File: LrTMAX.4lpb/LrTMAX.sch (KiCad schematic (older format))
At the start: 124 parts, among them J1 USB_C_Receptacle_USB2.0, J2 SM06B-SRSS-TB, Q1 2N7002, SW1 Tact_SW_8mm, SW10 EC11_SMD, SW11 EC11_SMD, SW12 EC11_SMD, SW13 EC11_SMD, SW14 EC11_SMD, SW15 EC11_SMD, SW16 EC11_SMD, SW17 EC11_SMD, SW2 Tact_SW_8mm, SW3 Tact_SW_8mm, SW4 Tact_SW_8mm, SW5 Tact_SW_8mm, SW6 Tact_SW_8mm, SW7 Tact_SW_8mm, SW8 Tact_SW_8mm, U1 STM32F072C8Tx, U3 SSD1306_OLED_0.91, U4 SPX3819M5-L3-3TR

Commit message: 0.55-pre3
Fix de-chatter cap. values to 22nF -> 100nF
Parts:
- C10, C11, C12, C13, C14, C15, C16, C17, C18, C19, C20, C21, C22, C23, C24, C25: value 22n -> 100n
- C30, C43, C44, C45: value 0.1u -> 100n
- C40, C41, C55: value 10n -> 100n
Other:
- moved on the sheet: C30
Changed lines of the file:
@@
 U 1 1 5C490EFE
 P 8000 1950
-F 0 "C40" H 8115 1996 50  0000 L CNN
-F 1 "10n" H 8115 1905 50  0000 L CNN
+F 0 "C40" H 7700 2000 50  0000 L CNN
+F 1 "100n" H 7700 1900 50  0000 L CNN
 F 2 "Capacitor_SMD:C_0603_1608Metric" H 8038 1800 50  0001 C CNN
 F 3 "~" H 8000 1950 50  0001 C CNN
@@
 P 9000 1600
 F 0 "C43" V 8950 1400 50  0000 C CNN
-F 1 "0.1u" V 8950 1750 50  0000 C CNN
+F 1 "100n" V 8950 1750 50  0000 C CNN
 F 2 "Capacitor_SMD:C_0603_1608Metric" H 9038 1450 50  0001 C CNN
 F 3 "~" H 9000 1600 50  0001 C CNN
@@
 P 9000 1900
 F 0 "C44" V 8950 1700 50  0000 C CNN
-F 1 "0.1u" V 8950 2050 50  0000 C CNN
+F 1 "100n" V 8950 2050 50  0000 C CNN
 F 2 "Capacitor_SMD:C_0603_1608Metric" H 9038 1750 50  0001 C CNN
 F 3 "~" H 9000 1900 50  0001 C CNN
@@
 P 9000 2200
 F 0 "C45" V 8950 2000 50  0000 C CNN
-F 1 "0.1u" V 8950 2350 50  0000 C CNN
+F 1 "100n" V 8950 2350 50  0000 C CNN
 F 2 "Capacitor_SMD:C_0603_1608Metric" H 9038 2050 50  0001 C CNN
 F 3 "~" H 9000 2200 50  0001 C CNN
@@
 P 9000 1200
 F 0 "C41" V 8950 1000 50  0000 C CNN
-F 1 "10n" V 8950 1350 50  0000 C CNN
+F 1 "100n" V 8950 1350 50  0000 C CNN
 F 2 "Capacitor_SMD:C_0603_1608Metric" H 9038 1050 50  0001 C CNN
 F 3 "~" H 9000 1200 50  0001 C CNN
@@
 L LrE-6-rescue:GND-power #PWR0104
 U 1 1 5C494D8B
-P 9250 2600
-F 0 "#PWR0104" H 9250 2350 50  0001 C CNN
-F 1 "GND" H 9255 2427 50  0000 C CNN
-F 2 "" H 9250 2600 50  0001 C CNN
-F 3 "" H 9250 2600 50  0001 C CNN
-	1    9250 2600
+P 9300 2500
+F 0 "#PWR0104" H 9300 2250 50  0001 C CNN
+F 1 "GND" H 9305 2327 50  0000 C CNN
+F 2 "" H 9300 2500 50  0001 C CNN
+F 3 "" H 9300 2500 50  0001 C CNN
+	1    9300 2500
 	1    0    0    -1
 $EndComp
 Wire Wire Line
-	9250 2600 9250 2400
+	9300 2500 9300 2400
 Wire Wire Line
-	9250 1200 9150 1200
+	9300 1200 9150 1200
 Wire Wire Line
-	9150 1400 9250 1400
-Connection ~ 9250 1400
+	9150 1400 9300 1400
+Connection ~ 9300 1400
 Wire Wire Line
-	9250 1400 9250 1200
+	9300 1400 9300 1200
 Wire Wire Line
-	9150 1600 9250 1600
-Connection ~ 9250 1600
+	9150 1600 9300 1600
+Connection ~ 9300 1600
 Wire Wire Line
-	9250 1600 9250 1400
+	9300 1600 9300 1400
 Wire Wire Line
-	9150 1900 9250 1900
+	9150 1900 9300 1900
 Wire Wire Line
-	9150 2200 9250 2200
-Connection ~ 9250 2200
+	9150 2200 9300 2200
+Connection ~ 9300 2200
 Wire Wire Line
-	9150 2400 9250 2400
-Connection ~ 9250 2400
+	9150 2400 9300 2400
+Connection ~ 9300 2400
 Wire Wire Line
-	9250 2400 9250 2200
+	9300 2400 9300 2200
 $Comp
 L LrE-6-rescue:MountingHole-Mechanical H1
@@
 $EndComp
 Wire Wire Line
-	9250 1600 9250 1900
+	9300 1600 9300 1900
 $Comp
 L LrE-6-rescue:GND-power #PWR0105
@@
 Wire Wire Line
 	8600 1900 8600 1050
-Connection ~ 9250 1900
+Connection ~ 9300 1900
 Wire Wire Line
 	8600 1900 8600 2450
 Wire Wire Line
-	9250 1900 9250 2200
+	9300 1900 9300 2200
 $Comp
 L LrE-6-rescue:+3V3-power #PWR0119
@@
 P 4350 1800
 F 0 "C18" H 4465 1846 50  0000 L CNN
-F 1 "22n" H 4400 1700 50  0000 L CNN
+F 1 "100n" H 4400 1700 50  0000 L CNN
 F 2 "Capacitor_SMD:C_0805_2012Metric" H 4388 1650 50  0001 C CNN
 F 3 "~" H 4350 1800 50  0001 C CNN
@@
 P 4700 1800
 F 0 "C19" H 4815 1846 50  0000 L CNN
-F 1 "22n" H 4750 1700 50  0000 L CNN
+F 1 "100n" H 4750 1700 50  0000 L CNN
 F 2 "Capacitor_SMD:C_0805_2012Metric" H 4738 1650 50  0001 C CNN
 F 3 "~" H 4700 1800 50  0001 C CNN
@@
 P 4450 3500
 F 0 "C20" H 4565 3546 50  0000 L CNN
-F 1 "22n" H 4500 3400 50  0000 L CNN
+F 1 "100n" H 4500 3400 50  0000 L CNN
 F 2 "Capacitor_SMD:C_0805_2012Metric" H 4488 3350 50  0001 C CNN
 F 3 "~" H 4450 3500 50  0001 C CNN
@@
 P 4800 3500
 F 0 "C21" H 4915 3546 50  0000 L CNN
-F 1 "22n" H 4850 3400 50  0000 L CNN
+F 1 "100n" H 4850 3400 50  0000 L CNN
 F 2 "Capacitor_SMD:C_0805_2012Metric" H 4838 3350 50  0001 C CNN
 F 3 "~" H 4800 3500 50  0001 C CNN
@@
 P 1550 1750
 F 0 "C10" H 1665 1796 50  0000 L CNN
-F 1 "22n" H 1600 1650 50  0000 L CNN
+F 1 "100n" H 1600 1650 50  0000 L CNN
 F 2 "Capacitor_SMD:C_0805_2012Metric" H 1588 1600 50  0001 C CNN
 F 3 "~" H 1550 1750 50  0001 C CNN
@@
 P 1900 1750
 F 0 "C11" H 2015 1796 50  0000 L CNN
-F 1 "22n" H 2000 1650 50  0000 L CNN
+F 1 "100n" H 2000 1650 50  0000 L CNN
 F 2 "Capacitor_SMD:C_0805_2012Metric" H 1938 1600 50  0001 C CNN
 F 3 "~" H 1900 1750 50  0001 C CNN
@@
 P 15050 1150
 F 0 "C55" H 15250 1250 50  0000 C CNN
-F 1 "10n" H 15250 1150 50  0000 C CNN
+F 1 "100n" H 15250 1150 50  0000 C CNN
 F 2 "Capacitor_SMD:C_0805_2012Metric" H 15088 1000 50  0001 C CNN
 F 3 "~" H 15050 1150 50  0001 C CNN
@@
 L LrE-6-rescue:C-Device C30
 U 1 1 5D54B231
-P 10850 3600
-F 0 "C30" H 10600 3650 50  0000 L CNN
-F 1 "0.1u" H 10600 3550 50  0000 L CNN
-F 2 "Capacitor_SMD:C_0805_2012Metric" H 10888 3450 50  0001 C CNN
-F 3 "~" H 10850 3600 50  0001 C CNN
-	1    10850 3600
+P 10850 3550
+F 0 "C30" H 11000 3600 50  0000 L CNN
+F 1 "100n" H 11000 3500 50  0000 L CNN
+F 2 "Capacitor_SMD:C_0805_2012Metric" H 10888 3400 50  0001 C CNN
+F 3 "~" H 10850 3550 50  0001 C CNN
+	1    10850 3550
 	1    0    0    -1
 $EndComp
@@
 P 4450 6900
 F 0 "C24" H 4565 6946 50  0000 L CNN
-F 1 "22n" H 4500 6800 50  0000 L CNN
+F 1 "100n" H 4500 6800 50  0000 L CNN
 F 2 "Capacitor_SMD:C_0805_2012Metric" H 4488 6750 50  0001 C CNN
 F 3 "~" H 4450 6900 50  0001 C CNN
@@
 P 4800 6900
 F 0 "C25" H 4915 6946 50  0000 L CNN
-F 1 "22n" H 4900 6800 50  0000 L CNN
+F 1 "100n" H 4900 6800 50  0000 L CNN
 F 2 "Capacitor_SMD:C_0805_2012Metric" H 4838 6750 50  0001 C CNN
 F 3 "~" H 4800 6900 50  0001 C CNN
@@
 P 1950 6850
 F 0 "C17" H 2065 6896 50  0000 L CNN
-F 1 "22n" H 2000 6750 50  0000 L CNN
+F 1 "100n" H 2000 6750 50  0000 L CNN
 F 2 "Capacitor_SMD:C_0805_2012Metric" H 1988 6700 50  0001 C CNN
 F 3 "~" H 1950 6850 50  0001 C CNN
@@
 P 1600 6850
 F 0 "C16" H 1715 6896 50  0000 L CNN
-F 1 "22n" H 1700 6750 50  0000 L CNN
+F 1 "100n" H 1700 6750 50  0000 L CNN
 F 2 "Capacitor_SMD:C_0805_2012Metric" H 1638 6700 50  0001 C CNN
 F 3 "~" H 1600 6850 50  0001 C CNN
@@
 P 1850 5100
 F 0 "C15" H 1965 5146 50  0000 L CNN
-F 1 "22n" H 1900 5000 50  0000 L CNN
+F 1 "100n" H 1900 5000 50  0000 L CNN
 F 2 "Capacitor_SMD:C_0805_2012Metric" H 1888 4950 50  0001 C CNN
 F 3 "~" H 1850 5100 50  0001 C CNN
@@
 P 1500 5100
 F 0 "C14" H 1615 5146 50  0000 L CNN
-F 1 "22n" H 1550 5000 50  0000 L CNN
+F 1 "100n" H 1550 5000 50  0000 L CNN
 F 2 "Capacitor_SMD:C_0805_2012Metric" H 1538 4950 50  0001 C CNN
 F 3 "~" H 1500 5100 50  0001 C CNN
@@
 P 1900 3450
 F 0 "C13" H 2015 3496 50  0000 L CNN
-F 1 "22n" H 1950 3350 50  0000 L CNN
+F 1 "100n" H 1950 3350 50  0000 L CNN
 F 2 "Capacitor_SMD:C_0805_2012Metric" H 1938 3300 50  0001 C CNN
 F 3 "~" H 1900 3450 50  0001 C CNN
@@
 P 1550 3450
 F 0 "C12" H 1665 3496 50  0000 L CNN
-F 1 "22n" H 1600 3350 50  0000 L CNN
+F 1 "100n" H 1600 3350 50  0000 L CNN
 F 2 "Capacitor_SMD:C_0805_2012Metric" H 1588 3300 50  0001 C CNN
 F 3 "~" H 1550 3450 50  0001 C CNN
@@
 P 4450 5200
 F 0 "C22" H 4565 5246 50  0000 L CNN
-F 1 "22n" H 4550 5100 50  0000 L CNN
+F 1 "100n" H 4550 5100 50  0000 L CNN
 F 2 "Capacitor_SMD:C_0805_2012Metric" H 4488 5050 50  0001 C CNN
 F 3 "~" H 4450 5200 50  0001 C CNN
@@
 P 4800 5200
 F 0 "C23" H 4915 5246 50  0000 L CNN
-F 1 "22n" H 4850 5100 50  0000 L CNN
+F 1 "100n" H 4850 5100 50  0000 L CNN
 F 2 "Capacitor_SMD:C_0805_2012Metric" H 4838 5050 50  0001 C CNN
 F 3 "~" H 4800 5200 50  0001 C CNN
@@
 L LrE-6-rescue:GND-power #PWR01
 U 1 1 60DE7033
-P 10850 3750
-F 0 "#PWR01" H 10850 3500 50  0001 C CNN
-F 1 "GND" H 10855 3577 50  0000 C CNN
-F 2 "" H 10850 3750 50  0001 C CNN
-F 3 "" H 10850 3750 50  0001 C CNN
-	1    10850 3750
+P 10850 3700
+F 0 "#PWR01" H 10850 3450 50  0001 C CNN
+F 1 "GND" H 10855 3527 50  0000 C CNN
+F 2 "" H 10850 3700 50  0001 C CNN
+F 3 "" H 10850 3700 50  0001 C CNN
+	1    10850 3700
 	1    0    0    -1
 $EndComp
@@
 	10300 3350 10850 3350
 Wire Wire Line
-	10850 3350 10850 3450
+	10850 3350 10850 3400
 Connection ~ 10300 3350
 Wire Wire Line

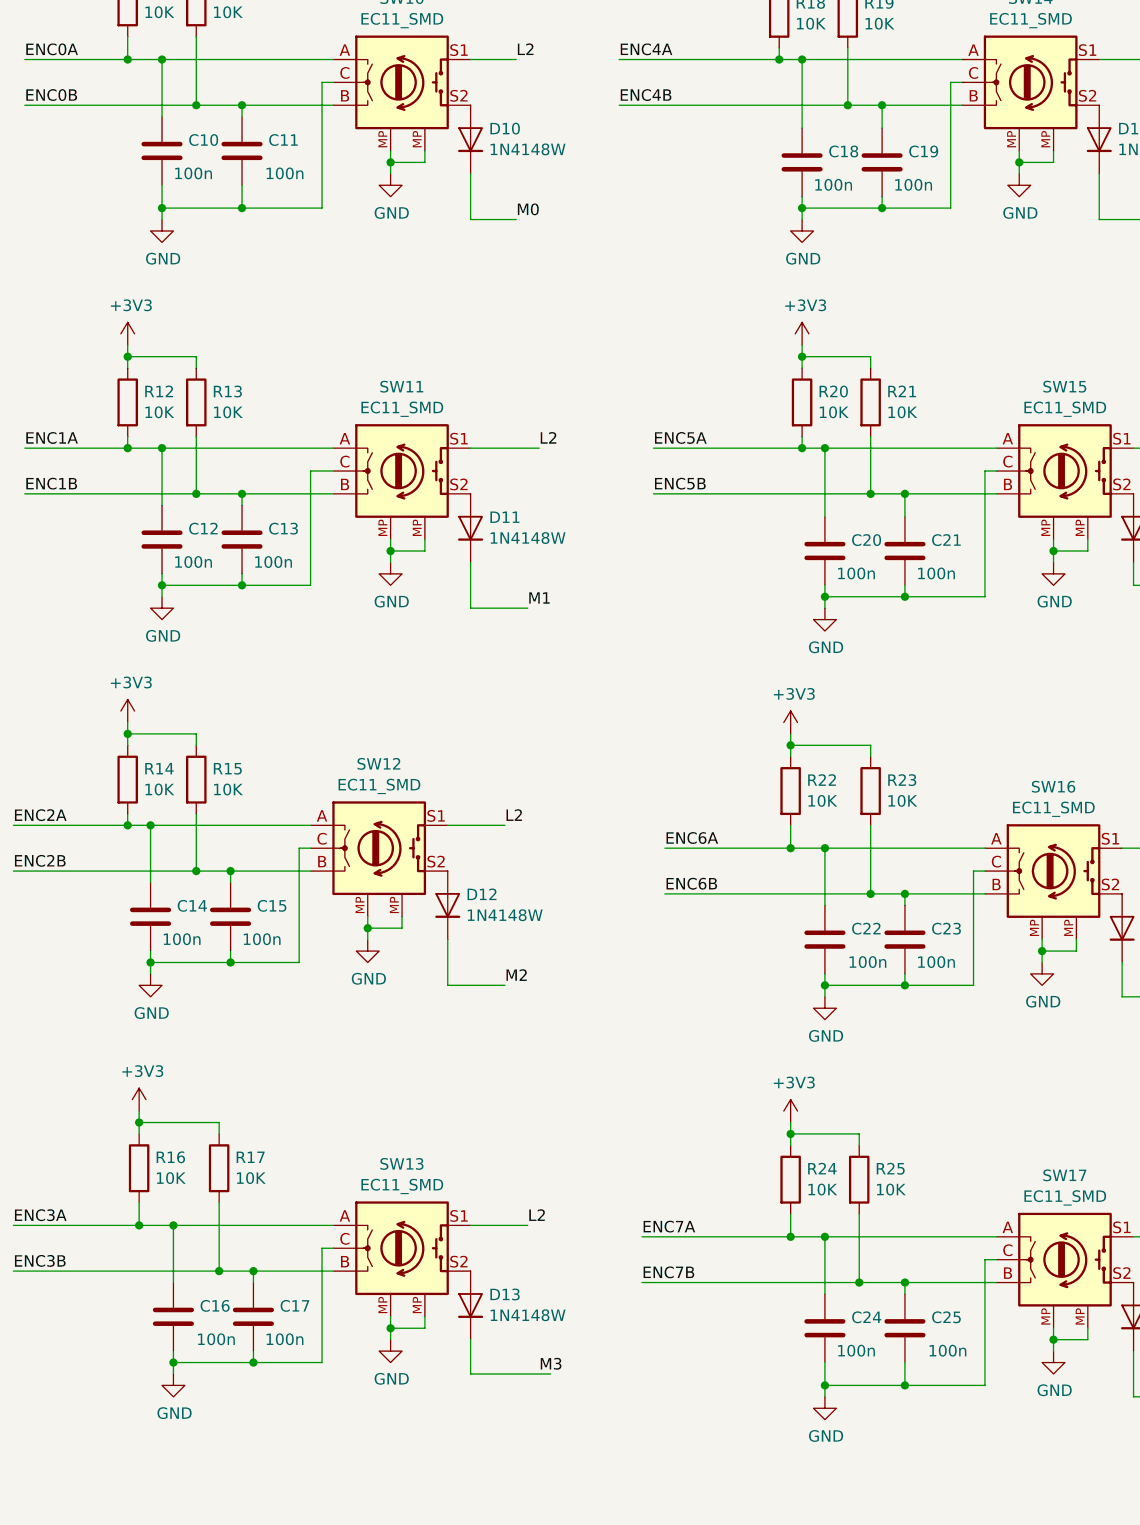
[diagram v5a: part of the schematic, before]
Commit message: 0.59-22
reverse de-chattter cap. to 22n
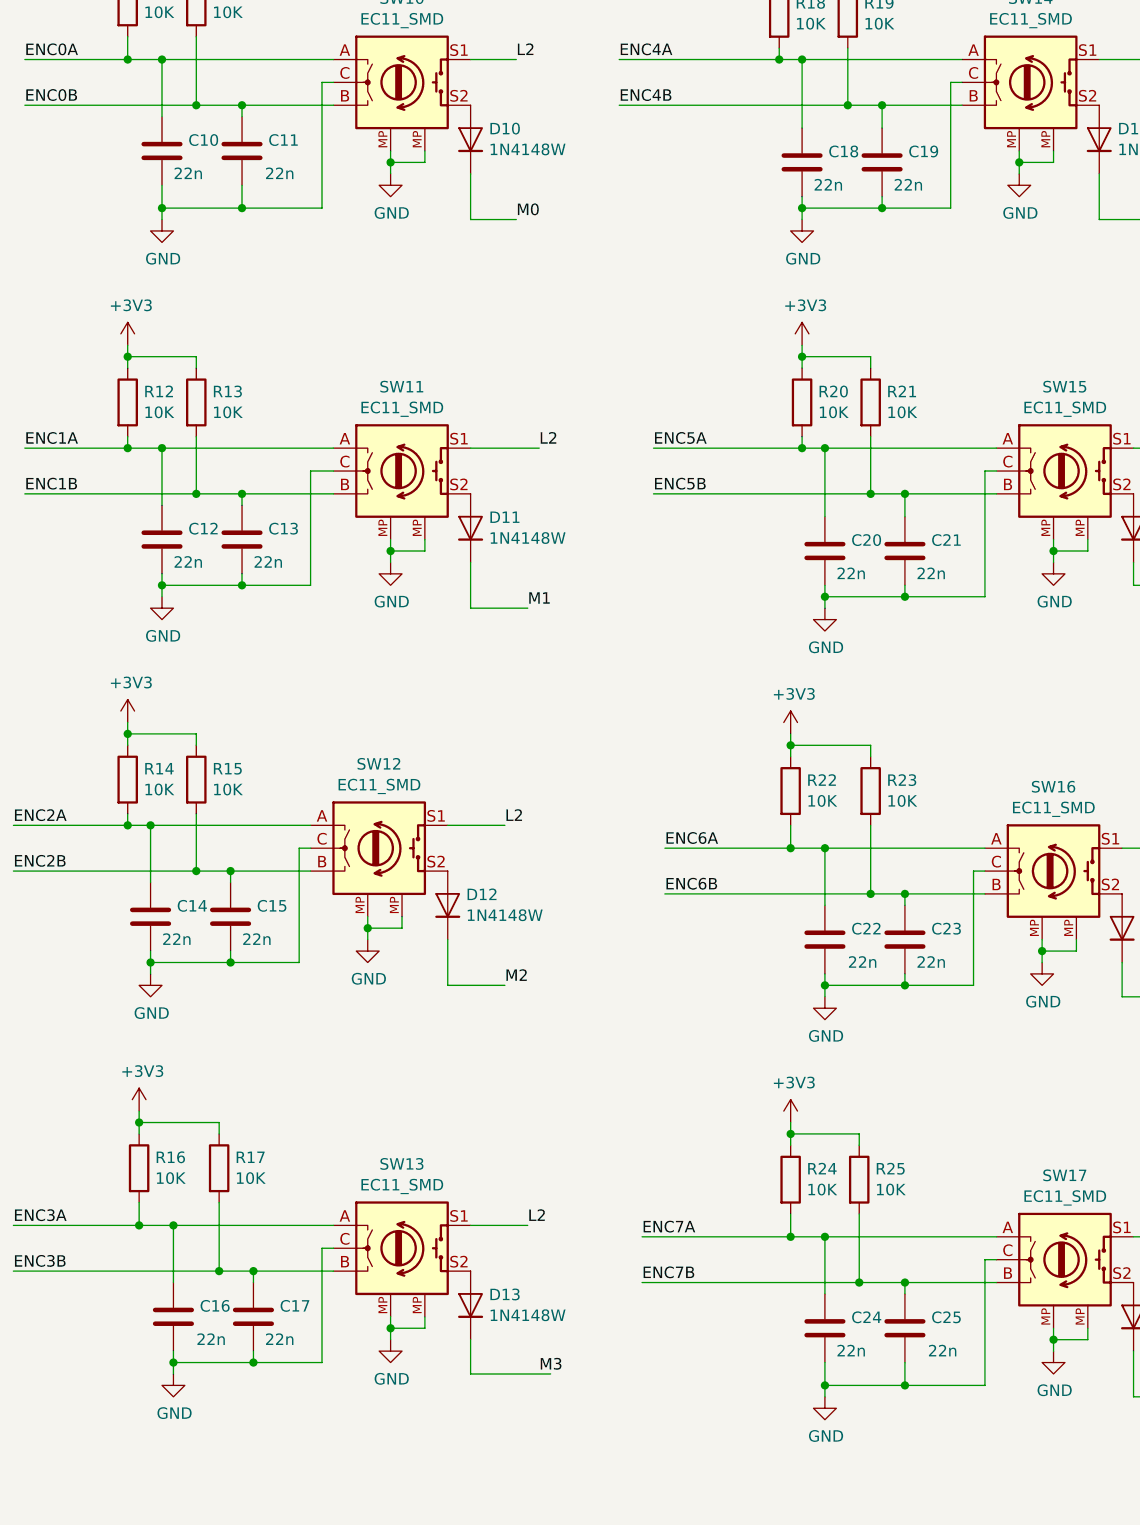
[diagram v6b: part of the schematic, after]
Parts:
- C10, C11, C12, C13, C14, C15, C16, C17, C18, C19, C20, C21, C22, C23, C24, C25: value 100n -> 22n
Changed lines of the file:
@@
 P 4350 1800
 F 0 "C18" H 4465 1846 50  0000 L CNN
-F 1 "100n" H 4400 1700 50  0000 L CNN
+F 1 "22n" H 4400 1700 50  0000 L CNN
 F 2 "Capacitor_SMD:C_0805_2012Metric" H 4388 1650 50  0001 C CNN
 F 3 "~" H 4350 1800 50  0001 C CNN
@@
 P 4700 1800
 F 0 "C19" H 4815 1846 50  0000 L CNN
-F 1 "100n" H 4750 1700 50  0000 L CNN
+F 1 "22n" H 4750 1700 50  0000 L CNN
 F 2 "Capacitor_SMD:C_0805_2012Metric" H 4738 1650 50  0001 C CNN
 F 3 "~" H 4700 1800 50  0001 C CNN
@@
 P 4450 3500
 F 0 "C20" H 4565 3546 50  0000 L CNN
-F 1 "100n" H 4500 3400 50  0000 L CNN
+F 1 "22n" H 4500 3400 50  0000 L CNN
 F 2 "Capacitor_SMD:C_0805_2012Metric" H 4488 3350 50  0001 C CNN
 F 3 "~" H 4450 3500 50  0001 C CNN
@@
 P 4800 3500
 F 0 "C21" H 4915 3546 50  0000 L CNN
-F 1 "100n" H 4850 3400 50  0000 L CNN
+F 1 "22n" H 4850 3400 50  0000 L CNN
 F 2 "Capacitor_SMD:C_0805_2012Metric" H 4838 3350 50  0001 C CNN
 F 3 "~" H 4800 3500 50  0001 C CNN
@@
 P 1550 1750
 F 0 "C10" H 1665 1796 50  0000 L CNN
-F 1 "100n" H 1600 1650 50  0000 L CNN
+F 1 "22n" H 1600 1650 50  0000 L CNN
 F 2 "Capacitor_SMD:C_0805_2012Metric" H 1588 1600 50  0001 C CNN
 F 3 "~" H 1550 1750 50  0001 C CNN
@@
 P 1900 1750
 F 0 "C11" H 2015 1796 50  0000 L CNN
-F 1 "100n" H 2000 1650 50  0000 L CNN
+F 1 "22n" H 2000 1650 50  0000 L CNN
 F 2 "Capacitor_SMD:C_0805_2012Metric" H 1938 1600 50  0001 C CNN
 F 3 "~" H 1900 1750 50  0001 C CNN
@@
 P 4450 6900
 F 0 "C24" H 4565 6946 50  0000 L CNN
-F 1 "100n" H 4500 6800 50  0000 L CNN
+F 1 "22n" H 4500 6800 50  0000 L CNN
 F 2 "Capacitor_SMD:C_0805_2012Metric" H 4488 6750 50  0001 C CNN
 F 3 "~" H 4450 6900 50  0001 C CNN
@@
 P 4800 6900
 F 0 "C25" H 4915 6946 50  0000 L CNN
-F 1 "100n" H 4900 6800 50  0000 L CNN
+F 1 "22n" H 4900 6800 50  0000 L CNN
 F 2 "Capacitor_SMD:C_0805_2012Metric" H 4838 6750 50  0001 C CNN
 F 3 "~" H 4800 6900 50  0001 C CNN
@@
 P 1950 6850
 F 0 "C17" H 2065 6896 50  0000 L CNN
-F 1 "100n" H 2000 6750 50  0000 L CNN
+F 1 "22n" H 2000 6750 50  0000 L CNN
 F 2 "Capacitor_SMD:C_0805_2012Metric" H 1988 6700 50  0001 C CNN
 F 3 "~" H 1950 6850 50  0001 C CNN
@@
 P 1600 6850
 F 0 "C16" H 1715 6896 50  0000 L CNN
-F 1 "100n" H 1700 6750 50  0000 L CNN
+F 1 "22n" H 1700 6750 50  0000 L CNN
 F 2 "Capacitor_SMD:C_0805_2012Metric" H 1638 6700 50  0001 C CNN
 F 3 "~" H 1600 6850 50  0001 C CNN
@@
 P 1850 5100
 F 0 "C15" H 1965 5146 50  0000 L CNN
-F 1 "100n" H 1900 5000 50  0000 L CNN
+F 1 "22n" H 1900 5000 50  0000 L CNN
 F 2 "Capacitor_SMD:C_0805_2012Metric" H 1888 4950 50  0001 C CNN
 F 3 "~" H 1850 5100 50  0001 C CNN
@@
 P 1500 5100
 F 0 "C14" H 1615 5146 50  0000 L CNN
-F 1 "100n" H 1550 5000 50  0000 L CNN
+F 1 "22n" H 1550 5000 50  0000 L CNN
 F 2 "Capacitor_SMD:C_0805_2012Metric" H 1538 4950 50  0001 C CNN
 F 3 "~" H 1500 5100 50  0001 C CNN
@@
 P 1900 3450
 F 0 "C13" H 2015 3496 50  0000 L CNN
-F 1 "100n" H 1950 3350 50  0000 L CNN
+F 1 "22n" H 1950 3350 50  0000 L CNN
 F 2 "Capacitor_SMD:C_0805_2012Metric" H 1938 3300 50  0001 C CNN
 F 3 "~" H 1900 3450 50  0001 C CNN
@@
 P 1550 3450
 F 0 "C12" H 1665 3496 50  0000 L CNN
-F 1 "100n" H 1600 3350 50  0000 L CNN
+F 1 "22n" H 1600 3350 50  0000 L CNN
 F 2 "Capacitor_SMD:C_0805_2012Metric" H 1588 3300 50  0001 C CNN
 F 3 "~" H 1550 3450 50  0001 C CNN
@@
 P 4450 5200
 F 0 "C22" H 4565 5246 50  0000 L CNN
-F 1 "100n" H 4550 5100 50  0000 L CNN
+F 1 "22n" H 4550 5100 50  0000 L CNN
 F 2 "Capacitor_SMD:C_0805_2012Metric" H 4488 5050 50  0001 C CNN
 F 3 "~" H 4450 5200 50  0001 C CNN
@@
 P 4800 5200
 F 0 "C23" H 4915 5246 50  0000 L CNN
-F 1 "100n" H 4850 5100 50  0000 L CNN
+F 1 "22n" H 4850 5100 50  0000 L CNN
 F 2 "Capacitor_SMD:C_0805_2012Metric" H 4838 5050 50  0001 C CNN
 F 3 "~" H 4800 5200 50  0001 C CNN
